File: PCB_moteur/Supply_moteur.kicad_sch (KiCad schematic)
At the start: 26 parts, among them J15 Vin_XT30PW-F, U13 L6981N33DR

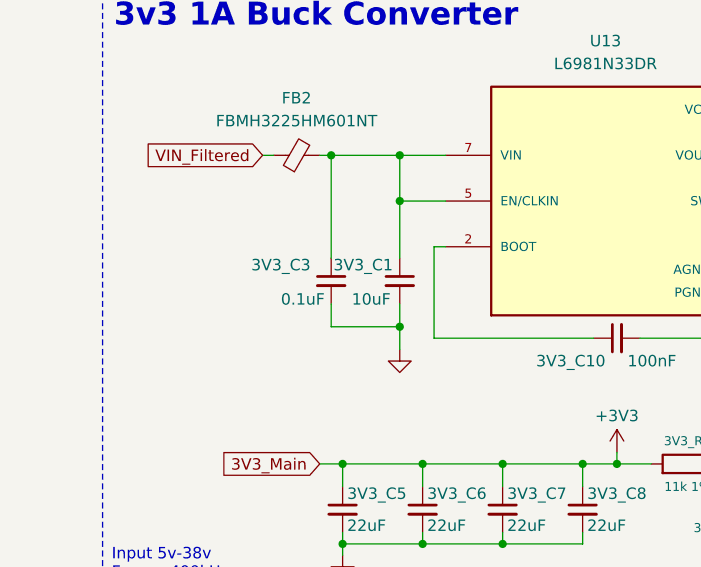
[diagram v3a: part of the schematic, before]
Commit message: fix: resistors + capacitances power supply
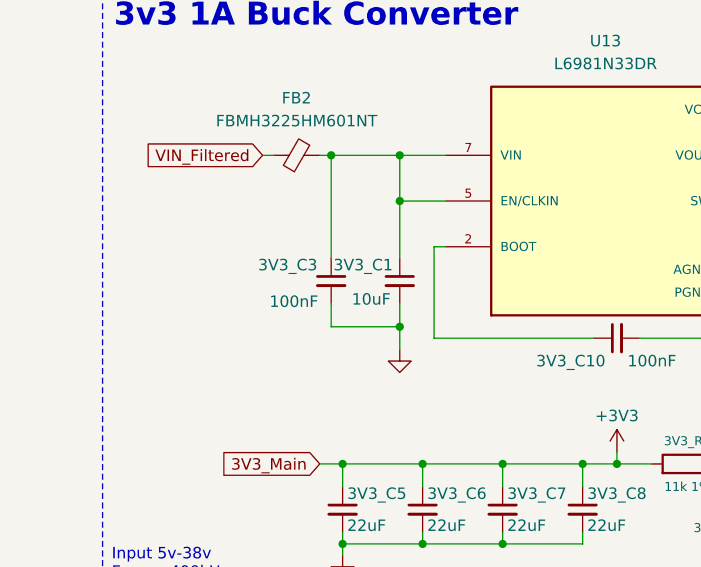
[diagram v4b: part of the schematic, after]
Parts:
- 3V3_C3: value 0.1uF -> 100nF
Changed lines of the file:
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@@
 		(dnp no)
 		(property "Reference" "3V3_C3"
-			(at 30.48 88.392 0)
+			(at 31.242 88.392 0)
 			(effects
 				(font
@@
 			)
 		)
-		(property "Value" "0.1uF"
-			(at 33.782 92.202 0)
+		(property "Value" "100nF"
+			(at 32.512 92.456 0)
 			(effects
 				(font

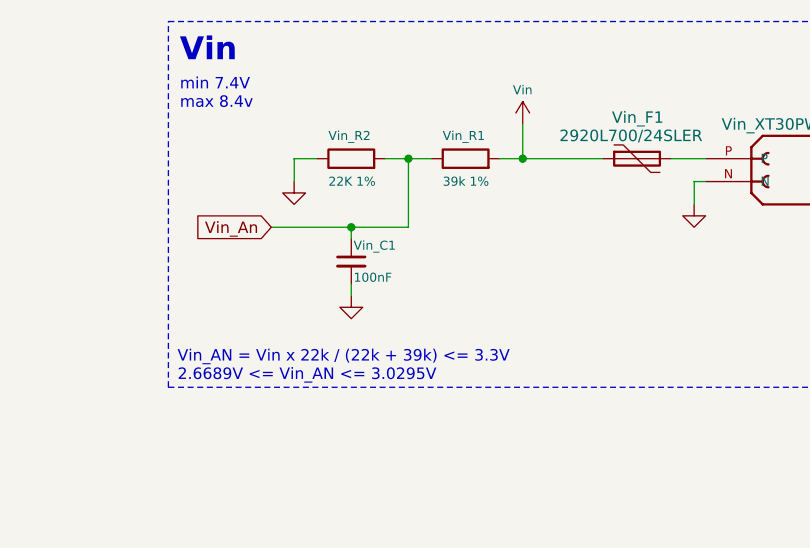
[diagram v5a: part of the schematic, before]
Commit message: fix: resistance ratios + typos
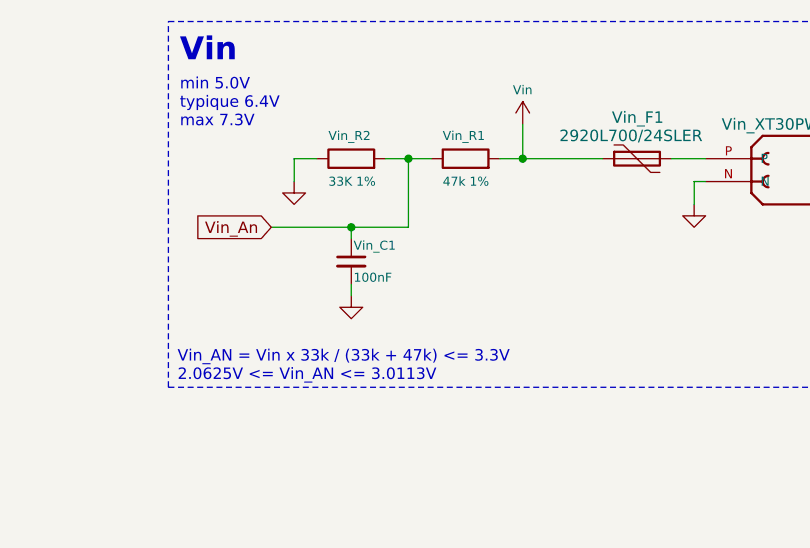
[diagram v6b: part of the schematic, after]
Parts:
- Vin_R1: value 39k 1% -> 47k 1%
- Vin_R2: value 22K 1% -> 33K 1%
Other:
- note added: "Vin_AN = Vin x 33k / (33k + 47k) <= 3.3V 2.0625V <= Vin_AN <= 3.0113V"
- note added: "min 5.0V typique 6.4V max 7.3V"
- note removed: "Vin_AN = Vin x 22k / (22k + 39k) <= 3.3V 2.6689V <= Vin_AN <= 3.0295V"
- note removed: "min 7.4V max 8.4v"
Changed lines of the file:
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@@
 		)
 	)
-	(text "Vin_AN = Vin x 22k / (22k + 39k) <= 3.3V\n2.6689V <= Vin_AN <= 3.0295V"
+	(text "Vin_AN = Vin x 33k / (33k + 47k) <= 3.3V\n2.0625V <= Vin_AN <= 3.0113V"
 		(exclude_from_sim no)
 		(at 208.026 51.054 0)
@@
 		)
 	)
-	(text "min 7.4V\nmax 8.4v"
+	(text "min 5.0V\ntypique 6.4V\nmax 7.3V"
 		(exclude_from_sim no)
 		(at 208.28 19.05 0)
@@
 			)
 		)
-		(property "Value" "22K 1%"
+		(property "Value" "33K 1%"
 			(at 224.79 30.48 90)
 			(effects
@@
 			)
 		)
-		(property "Value" "39k 1%"
+		(property "Value" "47k 1%"
 			(at 237.49 30.48 90)
 			(effects
